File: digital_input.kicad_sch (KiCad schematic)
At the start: 28 parts, among them J604 Conn_01x02, J605 Conn_01x02, J606 Conn_01x02, J607 Conn_01x02, U1101 74LVC1G17, U1102 74LVC1G17, U1103 74LVC1G17, U1104 74LVC1G17

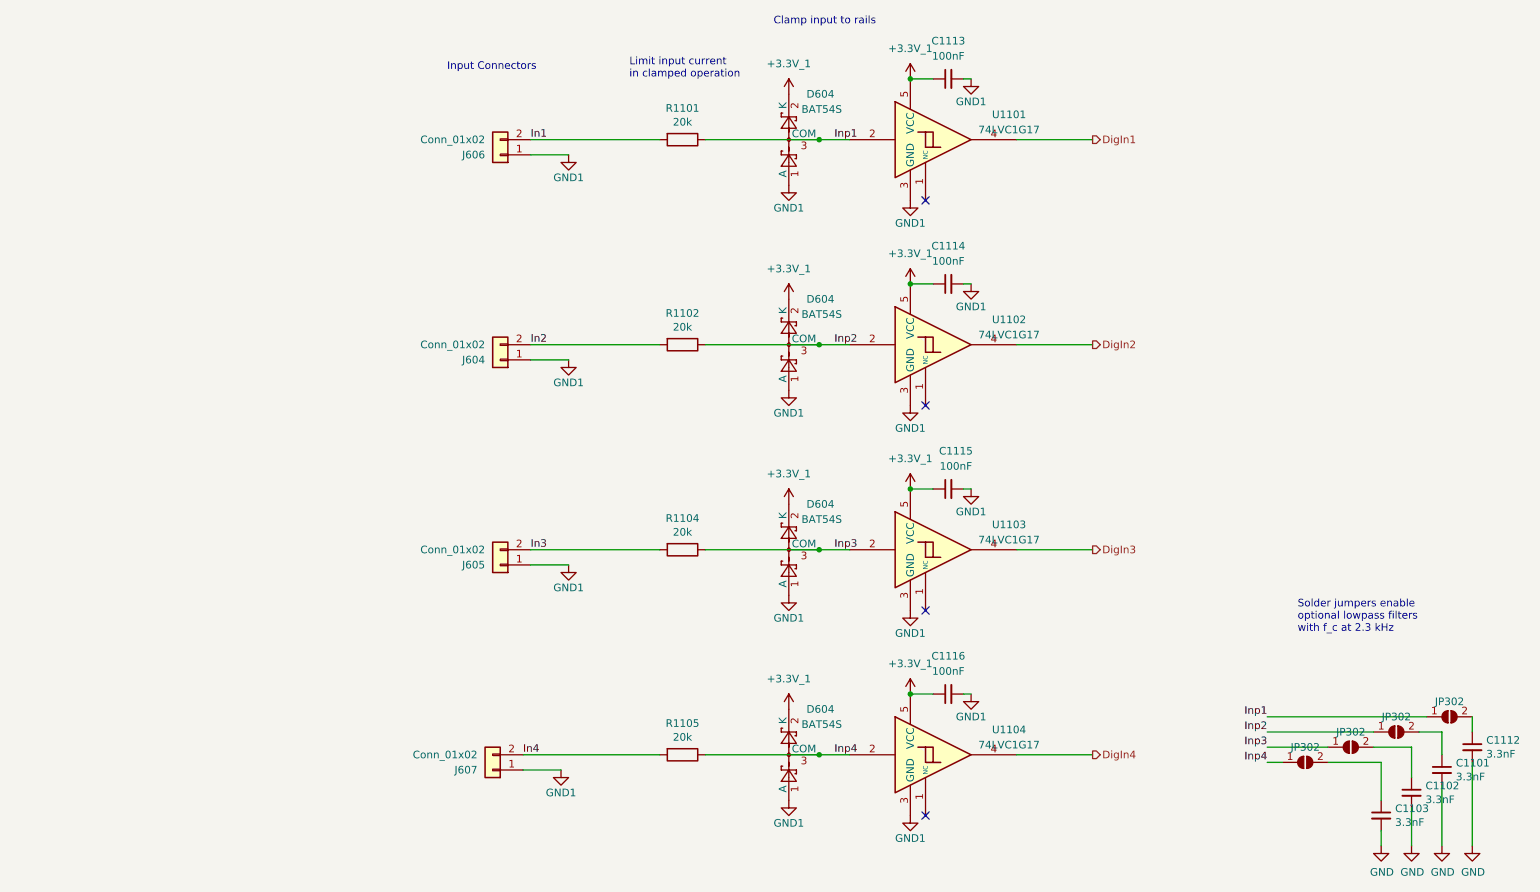
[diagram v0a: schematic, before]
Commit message: Implement HALMET v1.0.0 design changes
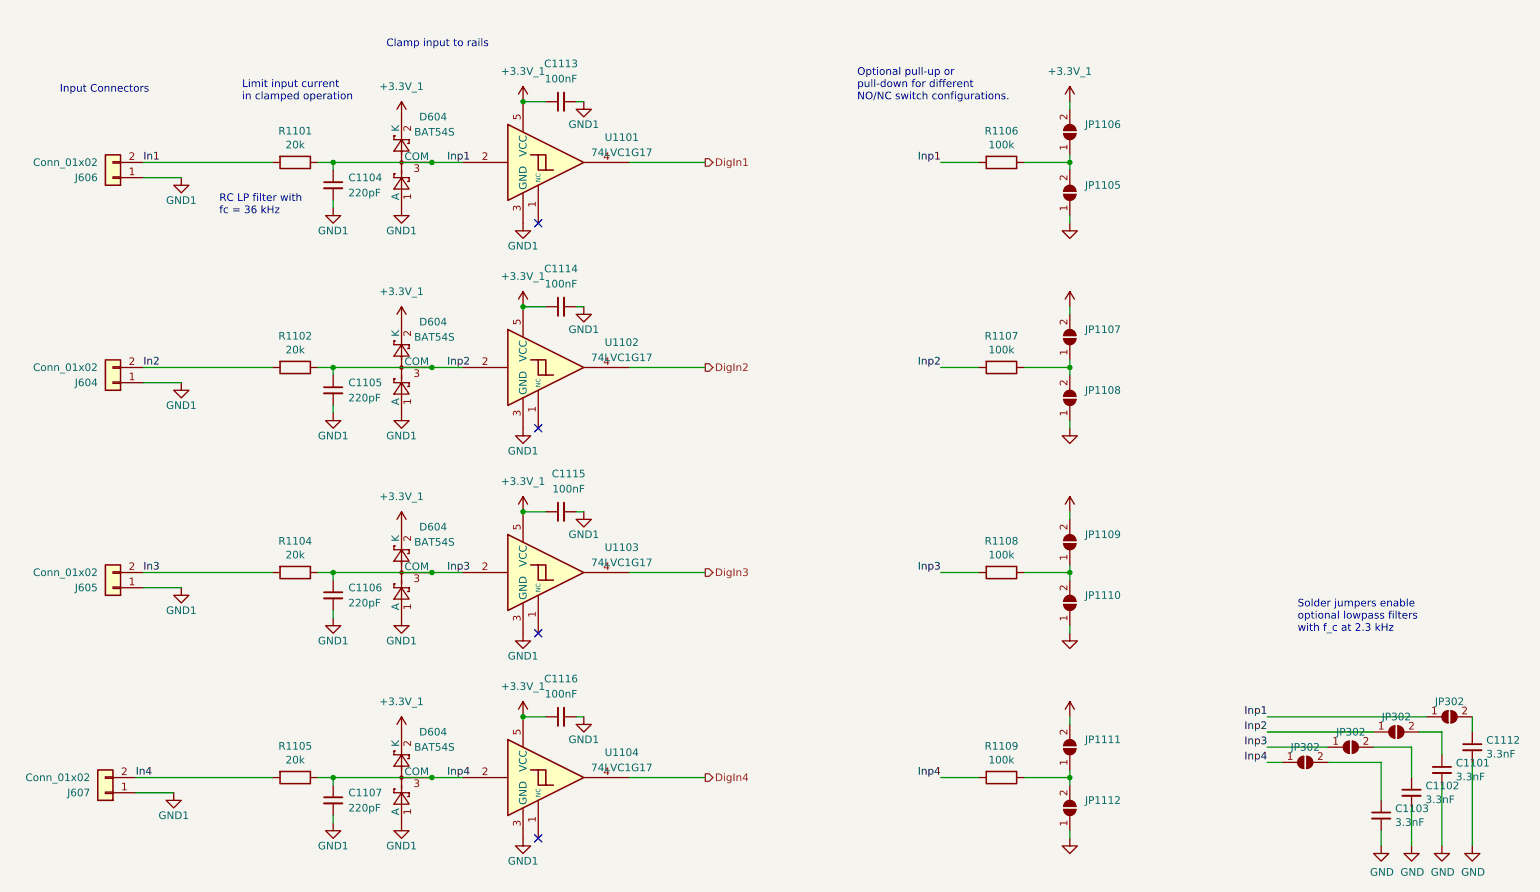
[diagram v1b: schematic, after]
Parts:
- added C1104, C1105, C1106, C1107: 220pF, Resistor_SMD:R_0402_1005Metric, symbol Device:C_Small
- added JP1105, JP1106, JP1107, JP1108, JP1109, JP1110, JP1111, JP1112: SolderJumper_2_Open, HALMET:SolderJumper-2_P1.3mm_Open_TrianglePad_Narrow, symbol Jumper:SolderJumper_2_Open
- added R1106, R1107, R1108, R1109: 100k, Resistor_SMD:R_0402_1005Metric, symbol Device:R
- D604: JLCPCB_CORRECTION (none) -> 0;0;180
- J604, J605, J606, J607: LCSC C8466 -> C8396
- R1101, R1102, R1104, R1105: footprint Resistor_SMD:R_0402_1005Metric -> Resistor_SMD:R_0603_1608Metric; LCSC C25765 -> C4184
- U1101, U1102, U1103, U1104: JLCPCB_CORRECTION (none) -> 0;0;270
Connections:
- net +3.3V_1: now also JP1106.2 (B), JP1107.2 (B), JP1109.2 (B), JP1111.2 (B)
- net GND1: now also C1104.2, C1105.2, C1106.2, C1107.2, JP1105.1 (A), JP1108.1 (A), JP1110.1 (A), JP1112.1 (A)
- net Inp1: now also C1104.1, R1106.2
- net Inp2: now also C1105.1, R1107.2
- net Inp3: now also C1106.1, R1108.2
- net Inp4: now also C1107.1, R1109.2
- new net: JP1105.2 (B), JP1106.1 (A), R1106.1
- new net: JP1107.1 (A), JP1108.2 (B), R1107.1
- new net: JP1111.1 (A), JP1112.2 (B), R1109.1
- new net: JP1109.1 (A), JP1110.2 (B), R1108.1
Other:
- note added: "Optional pull-up or pull-down for different NO/NC switch configurations."
- note added: "RC LP filter with fc = 36 kHz"
- title: Hat Labs Marine Engine/Tank interface (HALMET) -> Hat Labs Marine Engine & Tank interface (HALMET)
- moved on the sheet: C1113, C1114, C1115, C1116, D604, J604, J605, J606, J607, R1101, R1102, R1104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

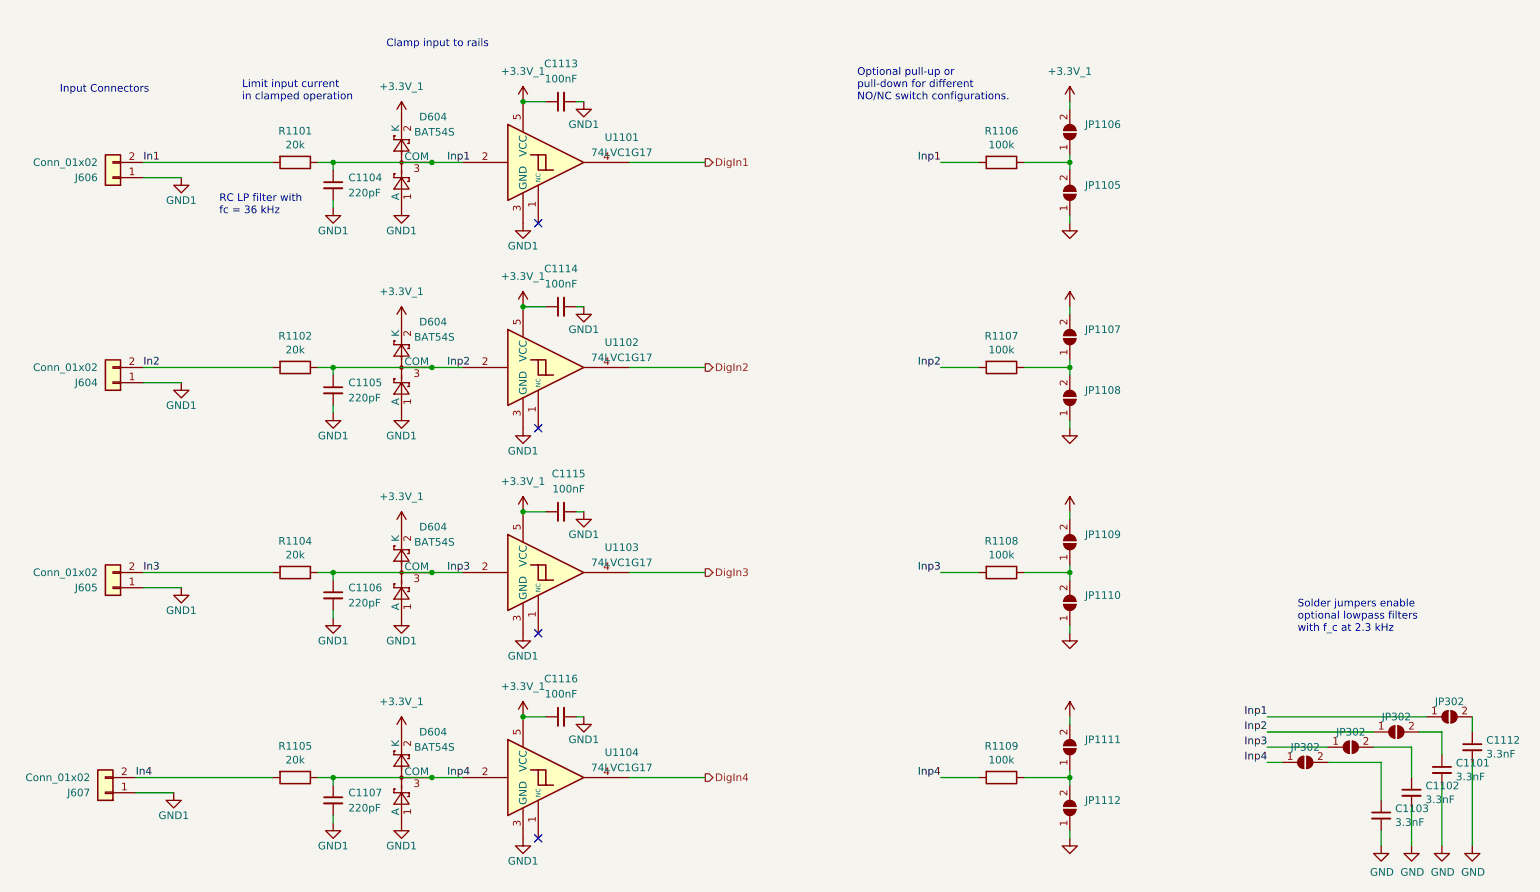
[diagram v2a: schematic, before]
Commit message: Save with a newer KiCad; change parts for availability; fix rotations
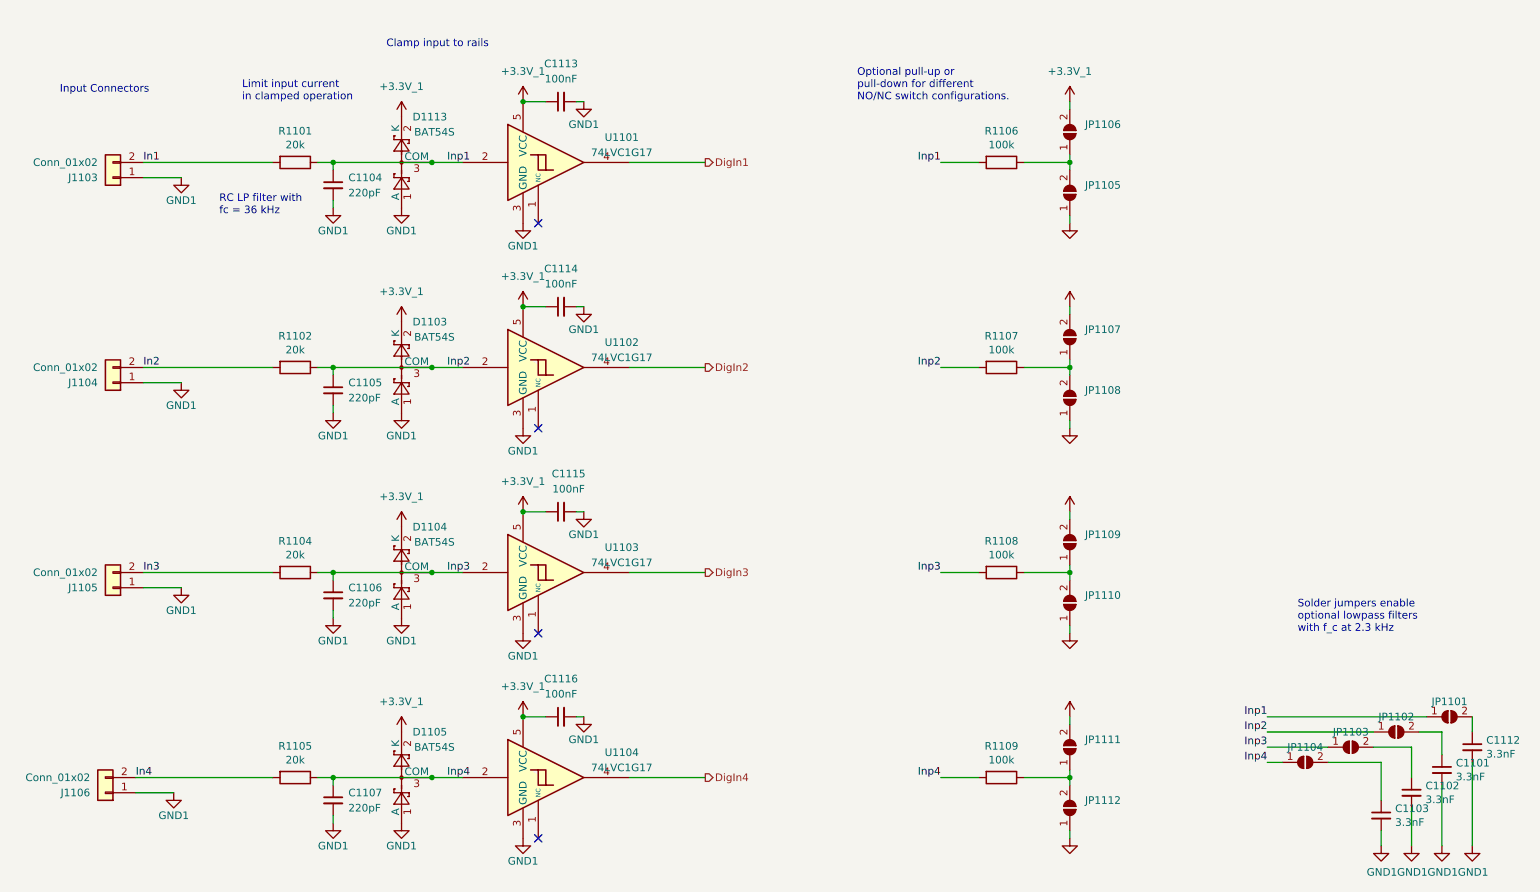
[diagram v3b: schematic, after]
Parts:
- J1103: renamed from J606; JLCPCB_CORRECTION (none) -> 1.905;0;180
- J1104: renamed from J604; JLCPCB_CORRECTION (none) -> 1.905;0;180
- J1105: renamed from J605; JLCPCB_CORRECTION (none) -> 1.905;0;180
- J1106: renamed from J607; JLCPCB_CORRECTION (none) -> 1.905;0;180
- U1101, U1102, U1103, U1104: LCSC C4945070 -> C212314
- renumbered D604 to D1103, D604 to D1104, D604 to D1105, D604 to D1113, JP302 to JP1101, JP302 to JP1102, JP302 to JP1103, JP302 to JP1104
